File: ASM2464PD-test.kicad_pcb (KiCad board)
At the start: 4 copper layers, 34.6 x 22 mm, 52 parts, among them J1 USB_C_Receptacle, J2 Bus_M.2_Socket_M, U2 SPI_SOIC-8, U3 SPI_DFN-8

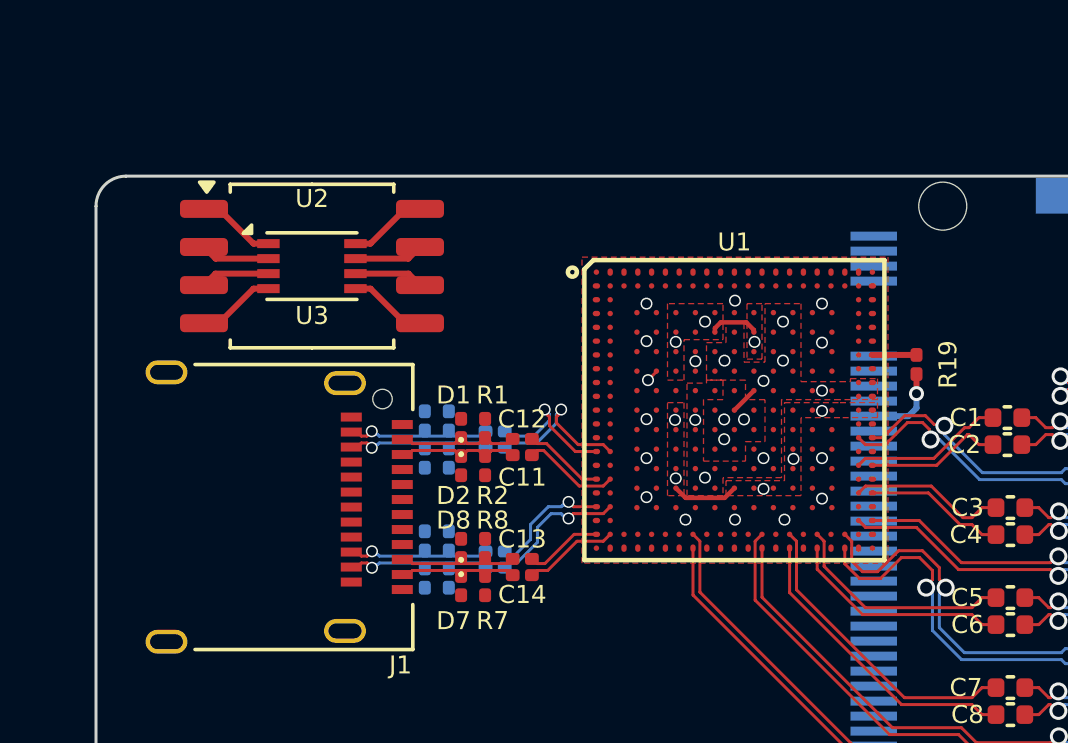
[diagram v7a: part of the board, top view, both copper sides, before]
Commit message: Adjusted ground fill under bga
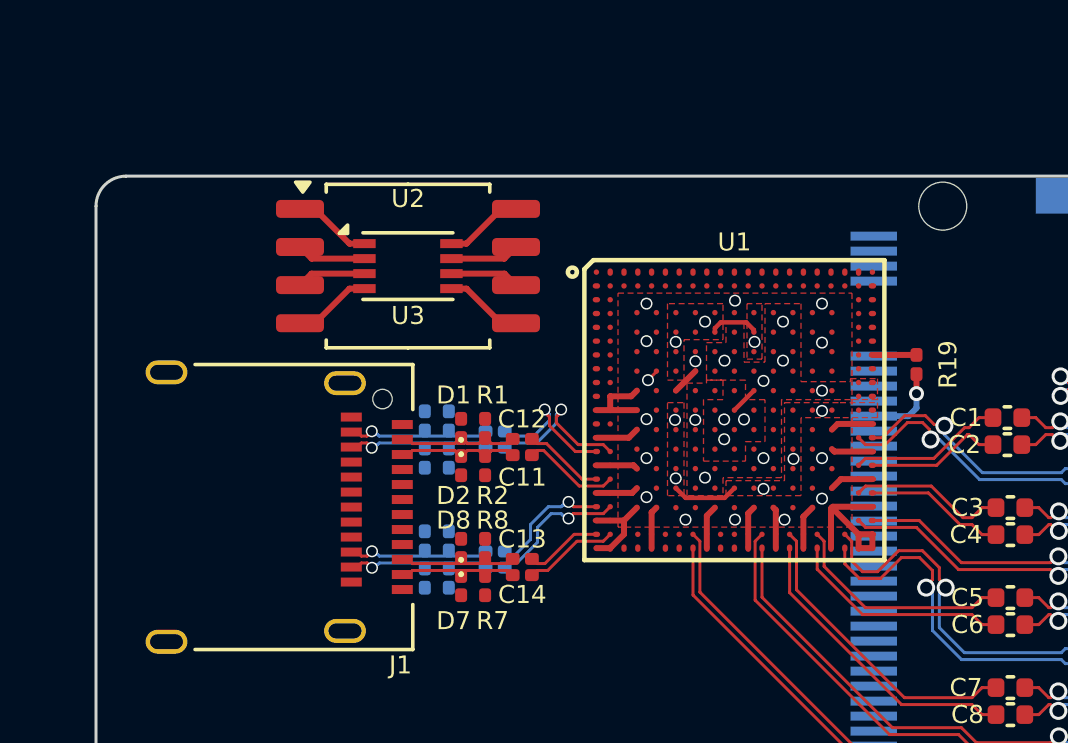
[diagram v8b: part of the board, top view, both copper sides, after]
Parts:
- moved U3 3.20 mm to (55.8, 73.0)
- moved U2 3.20 mm to (55.8, 73.0)
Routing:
- net GND: track 2.62 -> 31.0 mm
